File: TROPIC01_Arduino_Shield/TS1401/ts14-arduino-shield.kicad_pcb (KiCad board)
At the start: 2 copper layers, 58 x 53 mm, 17 parts, among them CON1 TROPIC01, IC1 TROPIC01_chip, IC2 TXU0304PWR

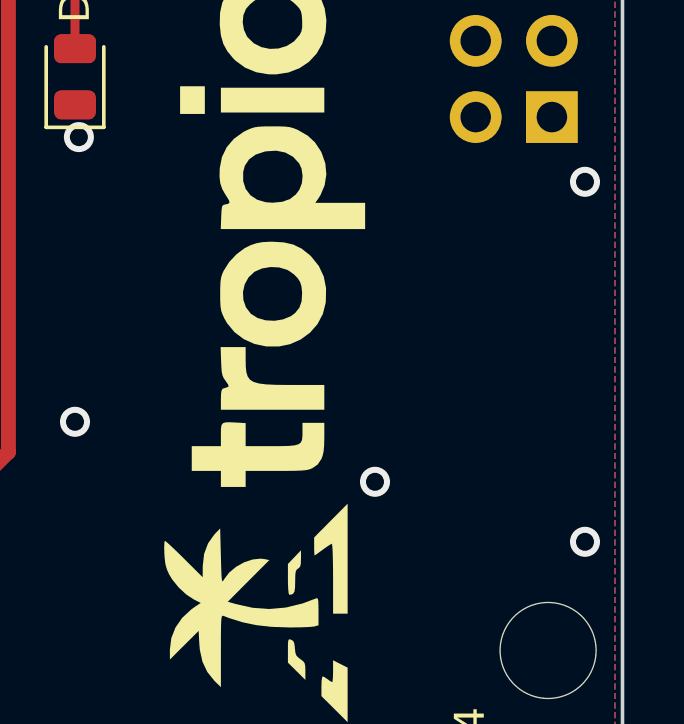
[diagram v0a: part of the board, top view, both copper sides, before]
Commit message: feat: Add silkscreen rectangle to TS1401
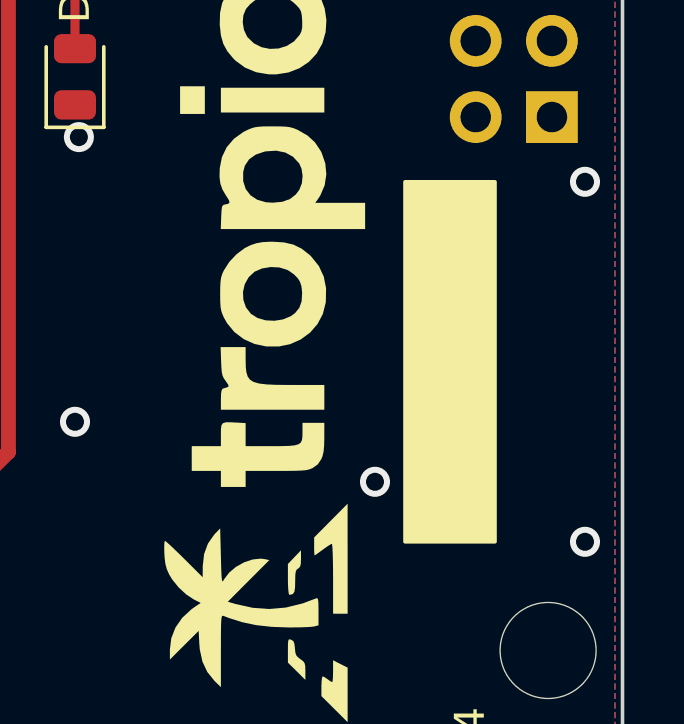
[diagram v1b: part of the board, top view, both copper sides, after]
